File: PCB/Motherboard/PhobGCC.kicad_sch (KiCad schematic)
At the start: 46 parts, among them J1 Conn_01x06_Female, J2 Conn_01x04_Female, J3 Conn_01x01_Male, J4 Conn_01x01_Male, J6 10118194-0001LF, SW1 A, SW10 Dup, SW11 Dright, SW12 Ddown, SW2 B, SW3 X, SW4 Y, SW5 Start, SW6 L, SW7 R, SW8 1825027-5, SW9 Dleft, U1 Teensy3.2, U2 2x DRV5053CAQLPGM Hall Effect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, U3 2.5V LDO

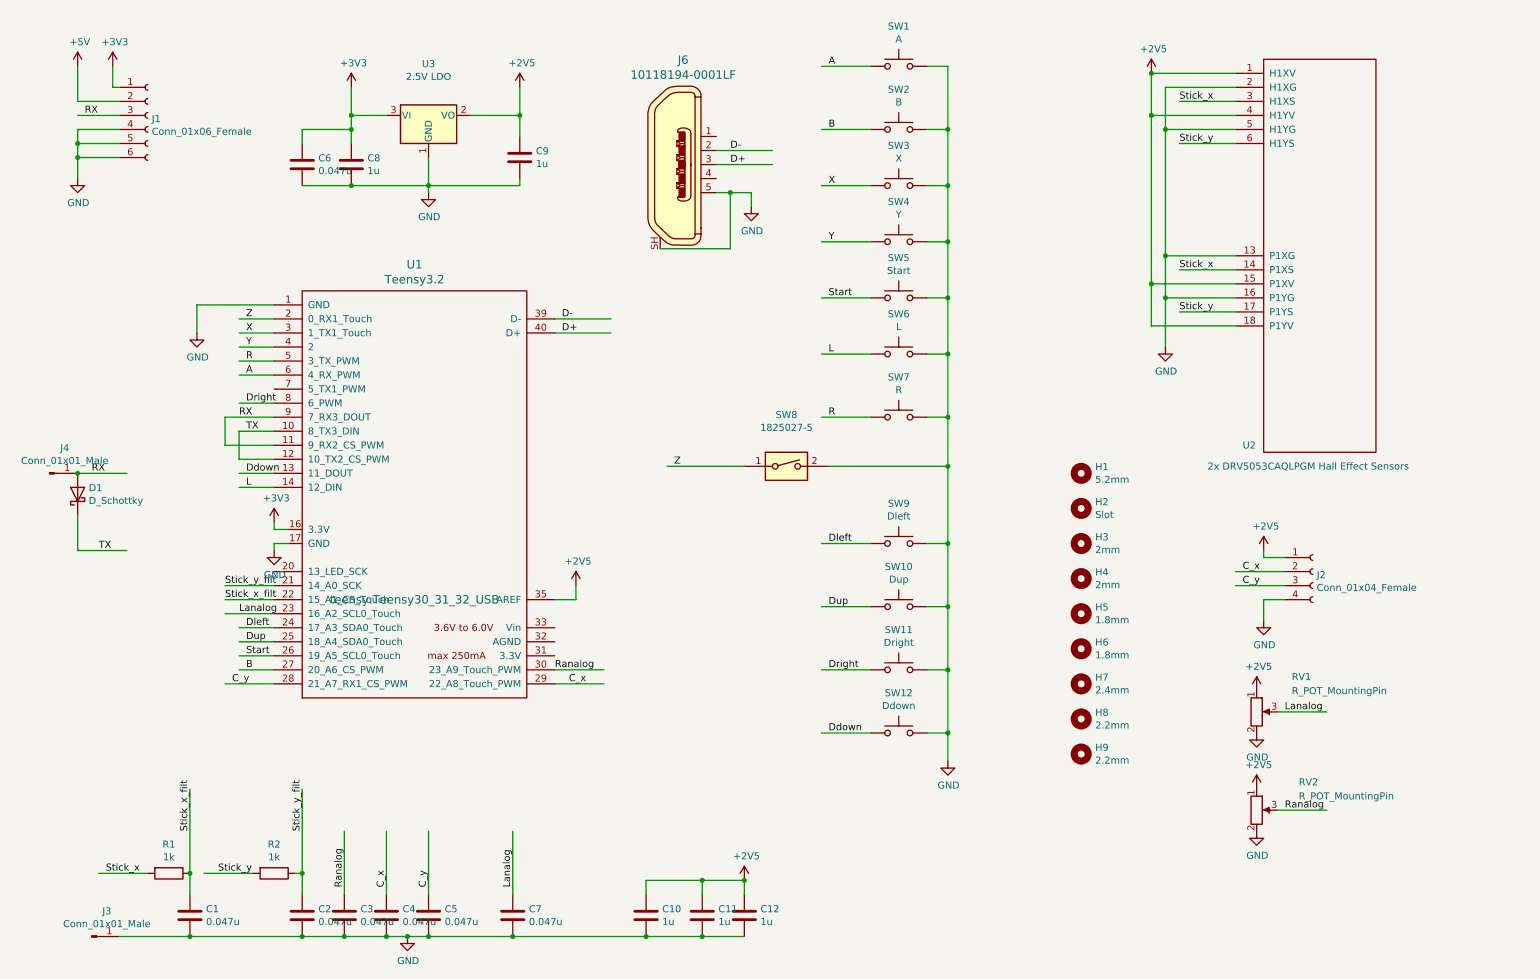
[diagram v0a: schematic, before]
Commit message: Commit with some of the major changes to the 1.2 board: Rumble, Optical Triggers, 5V, Mouse Buttons
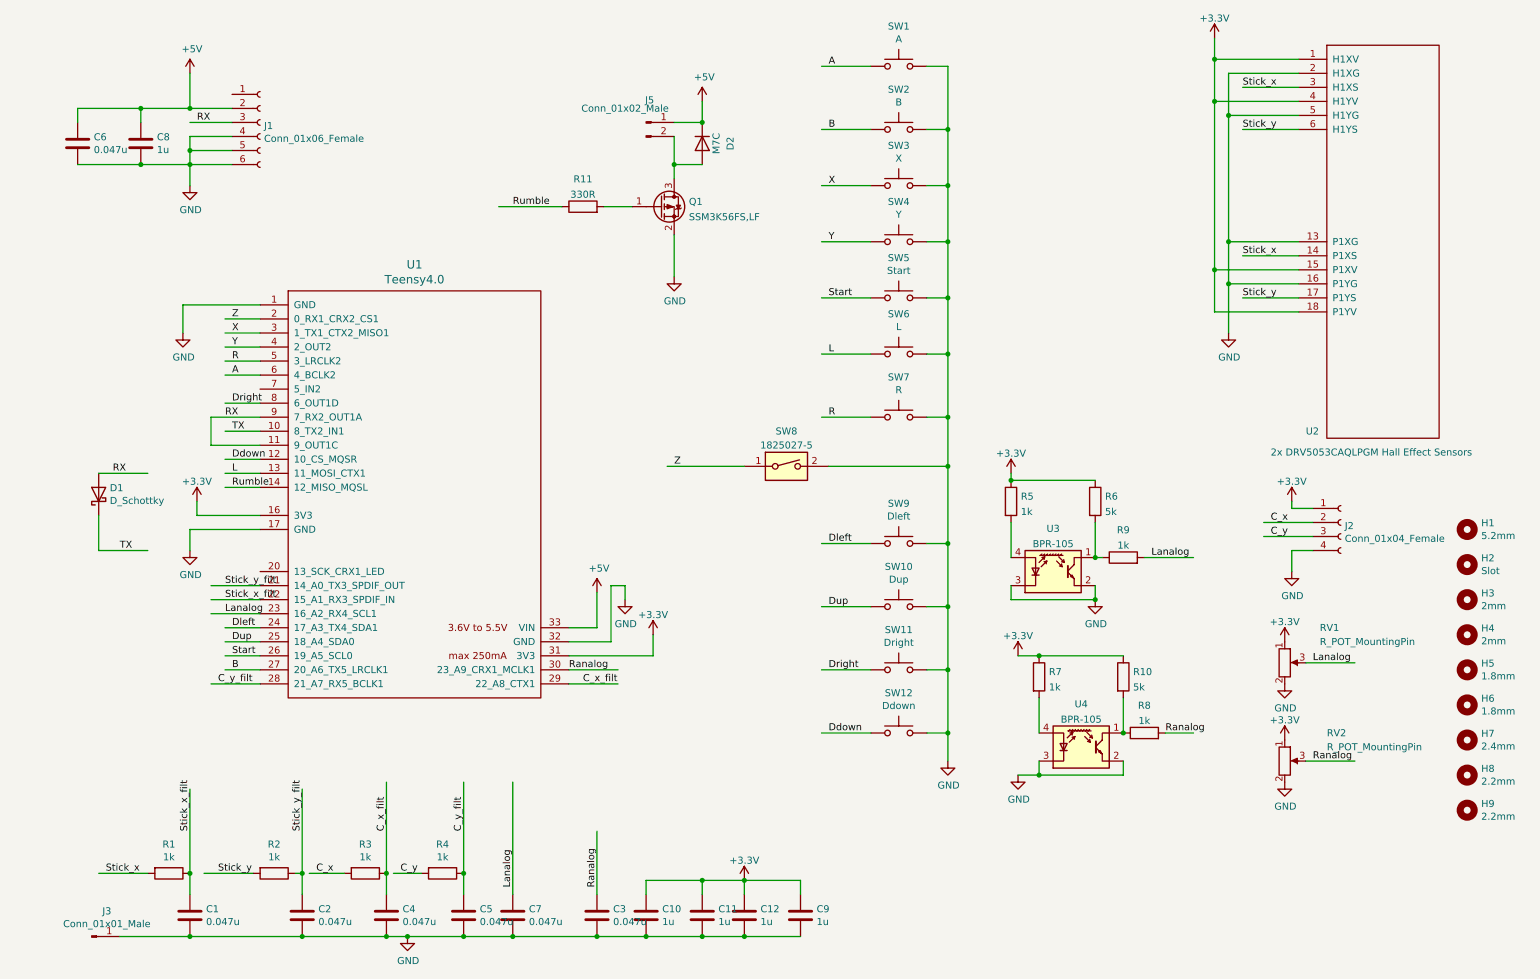
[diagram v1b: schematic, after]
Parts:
- removed J4: Conn_01x01_Male, Connector_PinHeader_2.54mm:PinHeader_1x01_P2.54mm_Vertical, symbol Connector:Conn_01x01_Male
- removed J6: 10118194-0001LF, digikeyUSB:USB_Micro_B_Female_10118194-0001LF, symbol dk_USB-DVI-HDMI-Connectors:10118194-0001LF
- removed U3: 2.5V LDO, Package_TO_SOT_SMD:SOT-23_Handsoldering, symbol Regulator_Linear:XC6206PxxxMR
- added D2: M7C, Diode_SMD:D_SOD-123F, symbol Device:D
- added J5: Conn_01x02_Male, Connector_PinHeader_2.54mm:PinHeader_1x02_P2.54mm_Vertical, symbol Connector:Conn_01x02_Male
- added Q1: SSM3K56FS,LF, Package_TO_SOT_SMD:SOT-416, symbol Transistor_FET:DMG2301L
- added R10, R6: 5k, Resistor_SMD:R_0603_1608Metric_Pad0.98x0.95mm_HandSolder, symbol Device:R
- added R11: 330R, Resistor_SMD:R_0603_1608Metric_Pad0.98x0.95mm_HandSolder, symbol Device:R
- added R3, R4, R5, R7, R8, R9: 1k, Resistor_SMD:R_0603_1608Metric_Pad0.98x0.95mm_HandSolder, symbol Device:R
- added U3, U4: BPR-105, Gamecube MB:Sharp_Microelectronics-GP2S60-MFG, symbol Sensor_Proximity:BPR-105
- C1, C2, C3, C4, C5, C6, C7: LCSC (none) -> C1604; MPN (none) -> 0603B222K500NT; Manufacturer (none) -> FH(Guangdong Fenghua Advanced Tech)
- C9: footprint Capacitors_SMD:C_0603_HandSoldering -> Capacitor_SMD:C_0603_1608Metric_Pad1.08x0.95mm_HandSolder
- R1: footprint Resistor_SMD:R_0603_1608Metric -> Resistor_SMD:R_0603_1608Metric_Pad0.98x0.95mm_HandSolder; LCSC (none) -> C25804; MPN (none) -> 0603WAF1002T5E; Manufacturer (none) -> UNI-ROYAL; Manufacturer PN (none) -> 0603WAF1002T5ECopy
- R2: footprint Resistor_SMD:R_0603_1608Metric -> Resistor_SMD:R_0603_1608Metric_Pad0.98x0.95mm_HandSolder; LCSC (none) -> C25804; MPN (none) -> 0603WAF1002T5E; Manufacturer (none) -> UNI-ROYAL
- SW1, SW2, SW3, SW4: footprint Gamecube MB:ABXY_layout_small_mask -> Gamecube MB:ABXY_layout_small_mask_omron_switch2
- U1: value Teensy3.2 -> Teensy4.0; footprint teensy:Teensy30_31_32_USB -> teensy:Teensy40_Edge_Pins; symbol teensy:Teensy3.2_USB -> teensy:Teensy4.0
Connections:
- net +3V3: now also C10.1, C11.1, C12.1, C9.1, J2.1 (Pin_1), RV1.1 (V+), RV2.1 (V+), U1.31 (3V3), U2.1 (H1XV), U2.15 (P1XV), U2.18 (P1YV), U2.4 (H1YV), R10.1, R5.1, R6.1, R7.1; no longer C6.1, C8.1, J1.1 (Pin_1)
- net +5V: now also C6.1, C8.1, U1.33 (VIN), D2.1 (K), J5.1 (Pin_1)
- net C_x: now also R3.2; no longer C4.1, U1.29 (22_A8_Touch_PWM)
- net C_y: now also R4.2; no longer C5.1, U1.28 (21_A7_RX1_CS_PWM)
- net Ddown: now also U1.12 (10_CS_MQSR); no longer U1.13 (11_DOUT)
- net GND: now also U1.32 (GND), Q1.2 (S), U3.2 (E), U3.3 (K), U4.2 (E), U4.3 (K)
- net L: now also U1.13 (11_MOSI_CTX1); no longer U1.14 (12_DIN)
- net Lanalog: now also R9.2
- net Ranalog: now also R8.2
- net TX: no longer U1.12 (10_TX2_CS_PWM)
- removed net +2V5: C10.1, C11.1, C12.1, C9.1, J2.1 (Pin_1), RV1.1 (V+), RV2.1 (V+), U1.35 (AREF), U2.1 (H1XV), U2.15 (P1XV), U2.18 (P1YV), U2.4 (H1YV)
- removed net D+: U1.40 (D+)
- removed net D-: U1.39 (D-)
- new net: R6.2, R9.1, U3.1 (C)
- new net: D2.2 (A), J5.2 (Pin_2), Q1.3 (D)
- new net: Q1.1 (G), R11.2
- new net: R10.2, R8.1, U4.1 (C)
- new net: R5.2, U3.4 (A)
- new net: R7.2, U4.4 (A)
- new net C_x_filt: C4.1, R3.1, U1.29 (22_A8_CTX1)
- new net C_y_filt: C5.1, R4.1, U1.28 (21_A7_RX5_BCLK1)
- new net Rumble: R11.1, U1.14 (12_MISO_MQSL)
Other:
- moved on the sheet: C3, C5, D1, H1, H2, H3, H4, H5, H6, H7, H8, H9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
